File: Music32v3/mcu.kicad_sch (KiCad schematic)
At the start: 6 parts, among them SW1 SW_Push, U1 ESP32-WROOM-32E__16MB_

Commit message: SD card and usb and power
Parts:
- added R23: 1M, Resistor_SMD:R_0402_1005Metric, symbol Device:R_Small
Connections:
- net GND: now also R23.1
- net TXD: now reaches U1.34 (RXD0)
- net RXD: now reaches U1.35 (TXD0)
- new net SD_SELECT: R23.2
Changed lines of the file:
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@@
+    (stroke (width 0) (type default))
+  )
+  (wire (pts (xy 97.79 106.68) (xy 95.25 106.68))
     (stroke (width 0) (type default))
   )
@@
     (stroke (width 0) (type default))
   )
+  (global_label "TXD" (shape passive) (at 121.92 101.6 180) (fields_autoplaced)
+    (effects (font (size 1.27 1.27)) (justify right))
+    (property "Intersheetrefs" "${INTERSHEET_REFS}" (at 116.6784 101.6 0)
+      (effects (font (size 1.27 1.27)) (justify right) hide)
+    )
+  )
+  (global_label "SD_DETECT" (shape passive) (at 90.17 97.79 180) (fields_autoplaced)
+    (effects (font (size 1.27 1.27)) (justify right))
+    (property "Intersheetrefs" "${INTERSHEET_REFS}" (at 78.1552 97.79 0)
+      (effects (font (size 1.27 1.27)) (justify right) hide)
+    )
+  )
+  (global_label "SD_SELECT" (shape passive) (at 95.25 106.68 180) (fields_autoplaced)
+    (effects (font (size 1.27 1.27)) (justify right))
+    (property "Intersheetrefs" "${INTERSHEET_REFS}" (at 83.2352 106.68 0)
+      (effects (font (size 1.27 1.27)) (justify right) hide)
+    )
+  )
+  (global_label "SD_PWR_EN" (shape passive) (at 97.79 100.33 180) (fields_autoplaced)
+    (effects (font (size 1.27 1.27)) (justify right))
+    (property "Intersheetrefs" "${INTERSHEET_REFS}" (at 85.1099 100.33 0)
+      (effects (font (size 1.27 1.27)) (justify right) hide)
+    )
+  )
+  (global_label "RXD" (shape passive) (at 121.92 99.06 180) (fields_autoplaced)
+    (effects (font (size 1.27 1.27)) (justify right))
+    (property "Intersheetrefs" "${INTERSHEET_REFS}" (at 116.376 99.06 0)
+      (effects (font (size 1.27 1.27)) (justify right) hide)
+    )
+  )
   (symbol (lib_id "Switch:SW_Push") (at 107.95 71.12 0) (unit 1)
     (in_bom yes) (on_board yes) (dnp no) (fields_autoplaced)
@@
     )
   )
+  (symbol (lib_id "Device:R_Small") (at 97.79 109.22 180) (unit 1)
+    (in_bom yes) (on_board yes) (dnp no)
+    (property "Reference" "R23" (at 93.98 105.41 0)
+      (effects (font (size 1.27 1.27)))
+    )
+    (property "Value" "1M" (at 93.472 107.95 0)
+      (effects (font (size 1.27 1.27)))
+    )
+    (property "Footprint" "Resistor_SMD:R_0402_1005Metric" (at 97.79 109.22 0)
+      (effects (font (size 1.27 1.27)) hide)
+    )
+    (property "Datasheet" "~" (at 97.79 109.22 0)
+      (effects (font (size 1.27 1.27)) hide)
+    )
+    (property "MPN_LCSC" "1" (at 97.79 109.22 90)
+      (effects (font (size 1.27 1.27)) hide)
+    )
+    (property "Price_LCSC" "0.0005" (at 97.79 109.22 90)
+      (effects (font (size 1.27 1.27)) hide)
+    )
+    (pin "1")
+    (pin "2")
+    (instances
+      (project "Power"
+        (path "/1288f273-4ee1-44e8-a86c-2adc0358dc71"
+          (reference "R23") (unit 1)
+        )
+      )
+      (project "Music_32_V2"
+        (path "/14681cc8-ddd4-43ff-b571-daca84d76d6b/4963a591-4c7d-4c5c-bcea-2e6cea395856"
+          (reference "R23") (unit 1)
+        )
+        (path "/14681cc8-ddd4-43ff-b571-daca84d76d6b/386f7fcb-de3c-43a3-99bd-dcf77f99c217"
+          (reference "R31") (unit 1)
+        )
+      )
+      (project "Music32v3"
+        (path "/492e826b-8900-4c12-8604-1c812b2e1995"
+          (reference "R13") (unit 1)
+        )
+        (path "/492e826b-8900-4c12-8604-1c812b2e1995/4998783d-7055-40b0-9979-647930a37834"
+          (reference "R13") (unit 1)
+        )
+        (path "/492e826b-8900-4c12-8604-1c812b2e1995/3c978059-9f1a-4ff6-9071-c1971133aa54"
+          (reference "R14") (unit 1)
+        )
+        (path "/492e826b-8900-4c12-8604-1c812b2e1995/af454206-d75b-4aff-be43-99164678694a"
+          (reference "R15") (unit 1)
+        )
+      )
+      (project "Phone"
+        (path "/9a44bf40-ccf4-4ff9-bb89-c8bc2c0cf19f/08dec41e-a7ac-46dd-ad42-4ddeee026110/46f942c4-bdd7-445d-bd75-6b4493769f4c"
+          (reference "R?") (unit 1)
+        )
+      )
+      (project "Ipod"
+        (path "/c4cf9ad0-abea-4c32-bb0b-367e5261d002"
+          (reference "R?") (unit 1)
+        )
+        (path "/c4cf9ad0-abea-4c32-bb0b-367e5261d002/683020cc-3f85-458f-8fb0-f668196e1562"
+          (reference "R22") (unit 1)
+        )
+      )
+      (project "power"
+        (path "/c90b3fe4-1e97-415b-a0f6-be34dcca7903"
+          (reference "R?") (unit 1)
+        )
+      )
+      (project "Power"
+        (path "/e4f8ce38-95ca-4021-bdd0-de4735b761e8"
+          (reference "R?") (unit 1)
+        )
+      )
+    )
+  )
   (symbol (lib_id "power:GND") (at 162.56 124.46 0) (unit 1)
     (in_bom yes) (on_board yes) (dnp no) (fields_autoplaced)
@@
         )
       )
+    )
+  )
+  (symbol (lib_id "power:GND") (at 97.79 111.76 0) (unit 1)
+    (in_bom yes) (on_board yes) (dnp no) (fields_autoplaced)
+    (property "Reference" "#PWR076" (at 97.79 118.11 0)
+      (effects (font (size 1.27 1.27)) hide)
+    )
+    (property "Value" "GND" (at 97.79 115.705 0)
+      (effects (font (size 1.27 1.27)))
+    )
+    (property "Footprint" "" (at 97.79 111.76 0)
+      (effects (font (size 1.27 1.27)) hide)
+    )
+    (property "Datasheet" "" (at 97.79 111.76 0)
+      (effects (font (size 1.27 1.27)) hide)
+    )
+    (pin "1")
+    (instances
+      (project "Music32v3"
+        (path "/492e826b-8900-4c12-8604-1c812b2e1995/af454206-d75b-4aff-be43-99164678694a"
+          (reference "#PWR076") (unit 1)
+        )
+      )

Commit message: Schematic
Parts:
- added R11, R12 (x7): 2K, Resistor_SMD:R_0402_1005Metric, symbol Device:R
- added R13 (x4): 10K, Resistor_SMD:R_0402_1005Metric, symbol Device:R
- added R17 (x2): 1M, Resistor_SMD:R_0402_1005Metric, symbol Device:R
- added SW3: PP, Music:TS3315A, symbol Switch:SW_Push
- added SW4: RW, Music:TS3315A, symbol Switch:SW_Push
- added SW5: FF, Music:TS3315A, symbol Switch:SW_Push
- added SW6: HOME, Music:TS3315A, symbol Switch:SW_Push
- added SW7, SW8: Vol+, Music:TSA002A3816B04, symbol Switch:SW_Push
- added SW9: Select, Music:TS3315A, symbol Switch:SW_Push
- added U1: Sk-3393, Music:SK-3393M-G1, symbol sk-3393m-g1:_SK-3393M-G1
- C1, C2: footprint (none) -> Capacitor_SMD:C_0805_2012Metric
- C3: footprint (none) -> Capacitor_SMD:C_0402_1005Metric
- R1: footprint (none) -> Resistor_SMD:R_0402_1005Metric
- SW1: value SW_Push -> RESET; footprint (none) -> Music:TS3315A
- U1: footprint ESP32-WROOM-32E__16MB_:XCVR_ESP32-WROOM-32E__16MB_ -> Music:ESP32-WROOM-32E
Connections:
- net +3.3V: now also R11.1, R12.1, R17.1, SW3.2, SW4.2, SW5.2, SW6.2, SW7.2, SW8.2
- net GND: now also R13.1, R17.1, SW9.2, U1.1, U1.6,7
- net EN: now reaches C3.1, R1.2, SW1.2, U1.3 (EN)
- net IO0: now reaches U1.25 (IO0)
- net IO0: now also SW9.1
- net CLK_UC: now reaches U1.30 (IO18)
- net MISO_UC: now reaches U1.31 (IO19)
- net MOSI_UC: now reaches U1.37 (IO23)
- new net: R12.1, SW4.1
- new net: R13.2, SW8.1
- new net: R12.1, R13.1, R13.1
- new net: R13.2, R13.2, SW7.1
- new net: R12.1, R12.1, SW5.1
- new net: R17.2, U1.5
- new net: R12.1, SW3.1
- new net: R12.1, R12.2
- new net BUTTONS: R12.2, R12.2, R12.2, R12.2, R12.2, R13.1, R13.2, SW6.1
- new net PWR/HOLD: R17.2, U1.3,4
- no-connect marks 0 -> 1
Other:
- note added: "HOME - 3.3 - 4095 FF - 3 - 3722 RW - 2.75 - 3412 PP - 2.357 - 2924 Vol+ - 1.94 - 2406 Vol- - 1.65 - 2047"
- note added: "Hold/Power switch"
- note added: "No adc 16,17,5,18,19,21,22,23"
- note added: "PWR is gnd for interrupt Hold is 1.65V for adc read"
- note added: "input only No internal pullup/pulldown"
- moved on the sheet: C3, R1, R23, SW1

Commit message: Reorganised
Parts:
- removed R12 (x6): 2K, Resistor_SMD:R_0402_1005Metric, symbol Device:R
- removed R13 (x4): 10K, Resistor_SMD:R_0402_1005Metric, symbol Device:R
- removed R17 (x2): 1M, Resistor_SMD:R_0402_1005Metric, symbol Device:R
- removed SW3: PP, Music:TS3315A, symbol Switch:SW_Push
- removed SW4: RW, Music:TS3315A, symbol Switch:SW_Push
- removed SW5: FF, Music:TS3315A, symbol Switch:SW_Push
- removed SW6: HOME, Music:TS3315A, symbol Switch:SW_Push
- removed SW7, SW8: Vol+, Music:TSA002A3816B04, symbol Switch:SW_Push
- removed SW9: Select, Music:TS3315A, symbol Switch:SW_Push
- removed U1: Sk-3393, Music:SK-3393M-G1, symbol sk-3393m-g1:_SK-3393M-G1
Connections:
- no-connect marks 1 -> 0
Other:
- note added: "Choose these based on layout"
- note removed: "HOME - 3.3 - 4095 FF - 3 - 3722 RW - 2.75 - 3412 PP - 2.357 - 2924 Vol+ - 1.94 - 2406 Vol- - 1.65 - 2047"
- note removed: "Hold/Power switch"
- note removed: "PWR is gnd for interrupt Hold is 1.65V for adc read"

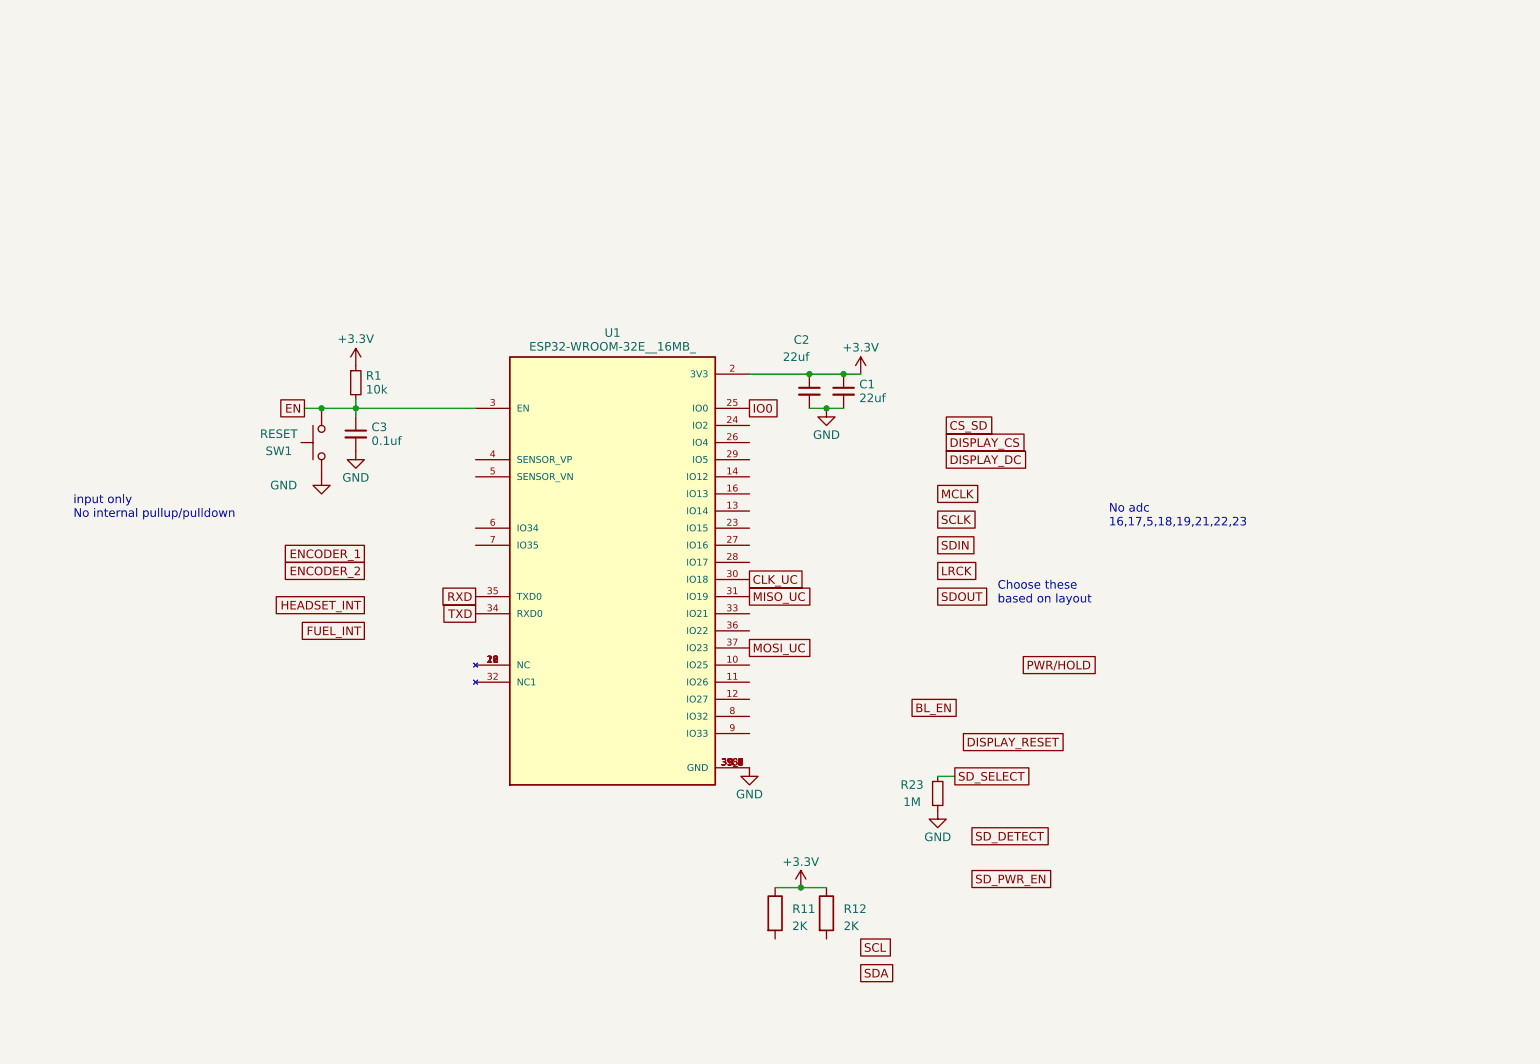
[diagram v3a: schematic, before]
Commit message: PCB outline
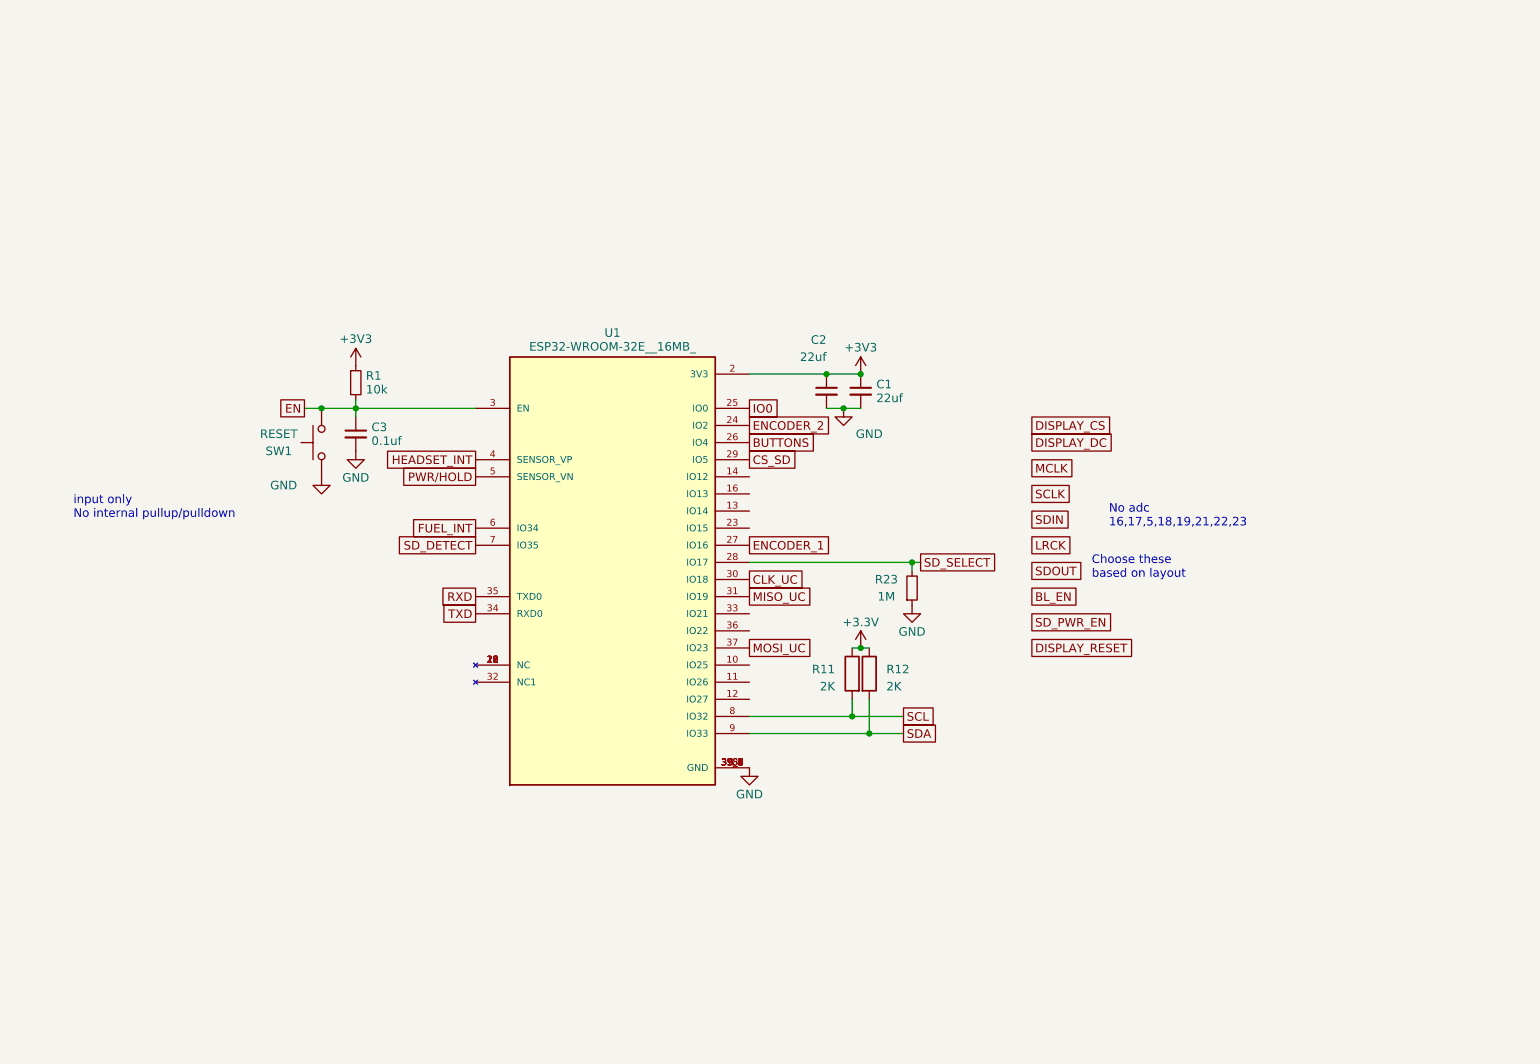
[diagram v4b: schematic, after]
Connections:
- net +3.3V: no longer C1.1, C2.1, R1.1, U1.2 (3V3)
- net CS_SD: now also U1.29 (IO5)
- net ENCODER_1: now also U1.27 (IO16)
- net ENCODER_2: now also U1.24 (IO2)
- net FUEL_INT: now also U1.6 (IO34)
- net HEADSET_INT: now also U1.4 (SENSOR_VP)
- net PWR/HOLD: now also U1.5 (SENSOR_VN)
- net SCL: now also R11.2, U1.8 (IO32)
- net SDA: now also R12.2, U1.9 (IO33)
- net SD_DETECT: now also U1.7 (IO35)
- net SD_SELECT: now also U1.28 (IO17)
- net BUTTONS: now reaches U1.26 (IO4)
- new net +3V3: C1.1, C2.1, R1.1, U1.2 (3V3)
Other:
- moved on the sheet: C1, C2, R11, R12, R23

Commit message: Board setup
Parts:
- added TP13: TestPoint, TestPoint:TestPoint_Loop_D2.50mm_Drill1.0mm, symbol Connector:TestPoint
- added TP6 (x3): TestPoint, TestPoint:TestPoint_Pad_D2.0mm, symbol Connector:TestPoint
- renumbered C3 to C5, C2 to C6, C1 to C7, R1 to R15, SW1 to SW8, U1 to U5
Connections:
- net +3.3V is gone; now on net +3V3: R11.1, R12.1
- net BL_EN: now also U5.24 (IO2)
- net DISPLAY_CS: now also U5.16 (IO13)
- net DISPLAY_DC: now also U5.23 (IO15)
- net DISPLAY_RESET: now also U5.13 (IO14)
- net EN: now also TP6.1
- net ENCODER_2: now also U5.28 (IO17); no longer U5.24 (IO2)
- net GND: now also TP13.1
- net HEADSET_INT: now also U5.5 (SENSOR_VN); no longer U5.4 (SENSOR_VP)
- net LRCK: now also U5.11 (IO26)
- net PWR/HOLD: now also U5.4 (SENSOR_VP); no longer U5.5 (SENSOR_VN)
- net SCL: now also TP6.1
- net SCLK: now also U5.14 (IO12)
- net SDA: now also TP6.1
- net SDIN: now also U5.12 (IO27)
- net SDOUT: now also U5.10 (IO25)
- net SD_PWR_EN: now also U5.36 (IO22)
- net SD_SELECT: now also U5.33 (IO21); no longer U5.28 (IO17)
- net TXD renamed MCLK_TXD
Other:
- moved on the sheet: R11, R12

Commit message: pdf schematic
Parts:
- C5: value 0.1uf -> 0.1uF
- R15: value 10k -> 10K
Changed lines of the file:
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@@
       (effects (font (size 1.27 1.27)) (justify left))
     )
-    (property "Value" "0.1uf" (at 106.4641 75.9603 0)
+    (property "Value" "0.1uF" (at 106.4641 75.9603 0)
       (effects (font (size 1.27 1.27)) (justify left))
     )
@@
   (symbol (lib_id "Device:R_Small") (at 104.14 67.31 0) (unit 1)
     (in_bom yes) (on_board yes) (dnp no) (fields_autoplaced)
-    (property "Reference" "R15" (at 105.6386 66.286 0)
+    (property "Reference" "R15" (at 106.68 66.675 0)
       (effects (font (size 1.27 1.27)) (justify left))
     )
-    (property "Value" "10k" (at 105.6386 68.334 0)
+    (property "Value" "10K" (at 106.68 69.215 0)
       (effects (font (size 1.27 1.27)) (justify left))
     )
